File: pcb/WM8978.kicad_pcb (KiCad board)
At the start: 2 copper layers, 1.7 x 7.7 mm, 72 parts, among them CN2 HEADPHONE 3.5mm, J2 JLINK SWD, SW1 RESET, U1 ATSAMD21E18A-A, U15 TLV1117LV33DCYR, U16 WM8978CGEFL/RV, U17 TPS2553DBVR, U18 SN74LVC1G125DBVR, Y1 12MHz / 3.3V / 50ppm

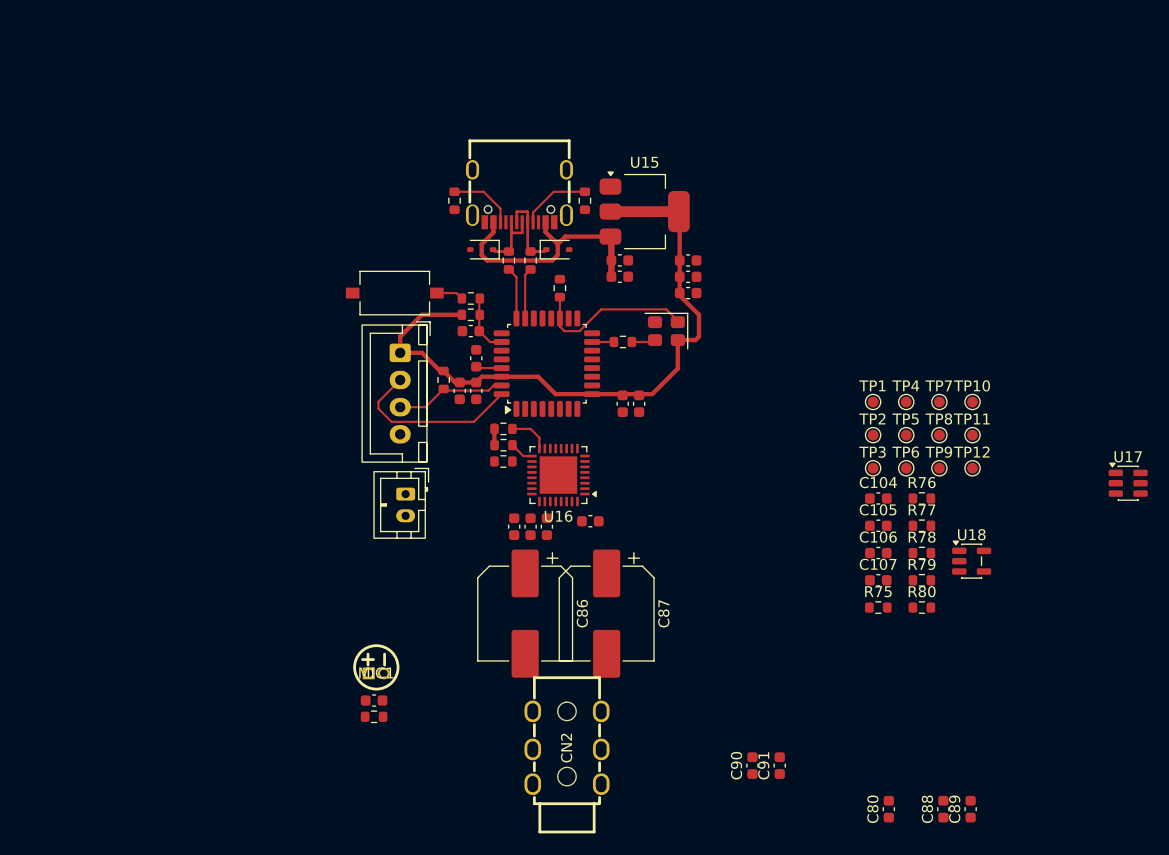
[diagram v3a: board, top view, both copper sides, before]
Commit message: 更新双时钟音频工程并整理中文原理图与检查资料
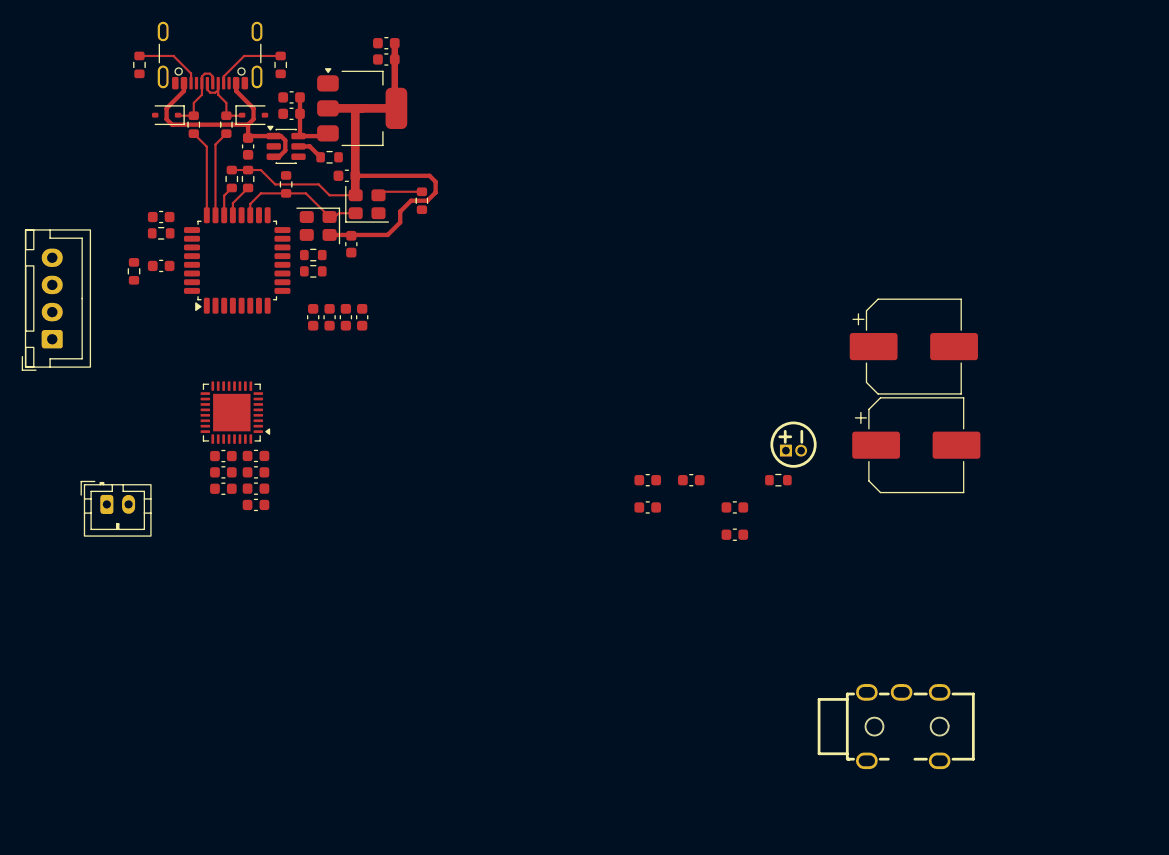
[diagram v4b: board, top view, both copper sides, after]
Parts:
- removed R62: 10k, Resistor_SMD:R_0603_1608Metric
- removed R72: 330R, Resistor_SMD:R_0603_1608Metric
- removed R77: 0R, Resistor_SMD:R_0603_1608Metric
- removed R79, R80: 100k, Resistor_SMD:R_0603_1608Metric
- removed SW1: RESET, Button_Switch_SMD:SW_Tactile_SPST_NO_Straight_CK_PTS636Sx25SMTRLFS
- removed TP1: RESET, TestPoint:TestPoint_Pad_D1.0mm
- removed TP10: SDA, TestPoint:TestPoint_Pad_D1.0mm
- removed TP11: SCL, TestPoint:TestPoint_Pad_D1.0mm
- removed TP12: FAULT, TestPoint:TestPoint_Pad_D1.0mm
- removed TP2: GND, TestPoint:TestPoint_Pad_D1.0mm
- removed TP3: RAW 5V, TestPoint:TestPoint_Pad_D1.0mm
- removed TP4: 5V, TestPoint:TestPoint_Pad_D1.0mm
- removed TP5: 3V3, TestPoint:TestPoint_Pad_D1.0mm
- removed TP6: CORE, TestPoint:TestPoint_Pad_D1.0mm
- removed TP7: MCLK, TestPoint:TestPoint_Pad_D1.0mm
- removed TP8: BCLK, TestPoint:TestPoint_Pad_D1.0mm
- removed TP9: LRCLK, TestPoint:TestPoint_Pad_D1.0mm
- removed U18: SN74LVC1G125DBVR, Package_TO_SOT_SMD:SOT-23-5
- added Y2: 12.288MHz / 3.3V / 50ppm, Oscillator:Oscillator_SMD_Abracon_ASE-4Pin_3.2x2.5mm, F.Cu at (112.0, 46.3)
- USB2: footprint WM8978-import-fps:USB_TYPE-C-16P -> WM8978-import-fps:USB_C_GCT_USB4105_GF_A
- moved U17 83.5 mm to (104.5, 41.0)
- moved C89 71.5 mm to (101.7, 74.0), turned to 0 degrees
- moved C88 69.8 mm to (101.7, 72.5), turned to 0 degrees
- moved C105 67.7 mm to (101.0, 41.0), turned to -90 degrees
- moved R78 65.6 mm to (108.5, 42.0)
- moved R75 60.5 mm to (107.0, 52.5), turned to 180 degrees
- moved R76 60.3 mm to (107.0, 51.0), turned to 180 degrees
- moved C104 57.2 mm to (110.1, 43.7), turned to 180 degrees
- moved C91 55.2 mm to (101.7, 71.0), turned to 0 degrees
- moved C90 53.9 mm to (101.7, 69.5), turned to 0 degrees
- moved MIC1 43.5 mm to (151.2, 69.0)
- moved C86 43.4 mm to (162.3, 59.4), turned to 0 degrees
- moved R68 43.1 mm to (149.8, 71.7), turned to 0 degrees
- moved C80 35.5 mm to (137.8, 74.2), turned to 0 degrees
- moved C77 34.4 mm to (105.0, 36.5), turned to 180 degrees
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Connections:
- C106 pad 1: /AVDD_3V3 -> +3V3
- C107 pad 1: /AVDD_3V3 -> +3V3
- CN2 pad 3: Net-(C87-Pad2) -> Net-(C86-Pad2)
- CN2 pad 4: Net-(C86-Pad2) -> Net-(C87-Pad2)
- R73 pad 1: /MCLK_BUF -> /AUDIO_OSC
- R73 pad 2: /I2S_MCLK -> /AUDIO_MCLK
- U1 pad 15: /I2S_MCLK -> /MCU_12M
- U16 pad 11: /I2S_MCLK -> /AUDIO_MCLK
- U16 pad 18: /MODE -> GND
- U16 pad 31: /AVDD_3V3 -> +3V3
- U17 pad 4: Net-(U17-~{FAULT}) -> unconnected-(U17-~{FAULT}-Pad4)
- Y1 pad 3: /MCLK_XO -> /MCU_12M
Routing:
- net /VBUS_RAW: track 0.00 -> 23.7 mm
- net /VBUS_5V: track 23.6 -> 6.43 mm
- net /SWDIO: track 16.4 -> 0.00 mm
- net /SWCLK: track 10.3 -> 0.00 mm
- net +3V3: track 61.5 -> 53.2 mm
- net /MCU_RESET_N: track 5.50 -> 0.00 mm
- net /AUDIO_OSC: track 0.00 -> 4.13 mm
- net /USB_DP: track 4.80 -> 8.01 mm
- net /USB_DM: track 4.72 -> 7.93 mm
- net /AUDIO_CLK_EN: track 15.1 -> 12.2 mm
- net Net-(R72-Pad2): track 2.51 -> 0.00 mm
- net Net-(U17-ILIM): track 0.00 -> 2.45 mm
- net /VDDCORE: track 2.39 -> 0.00 mm
- net (no net): track 2.20 -> 0.00 mm
- net /I2S_MCLK: track 2.01 -> 0.00 mm
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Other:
- board size 1.7 x 7.7 mm -> 7.7 x 1.7 mm

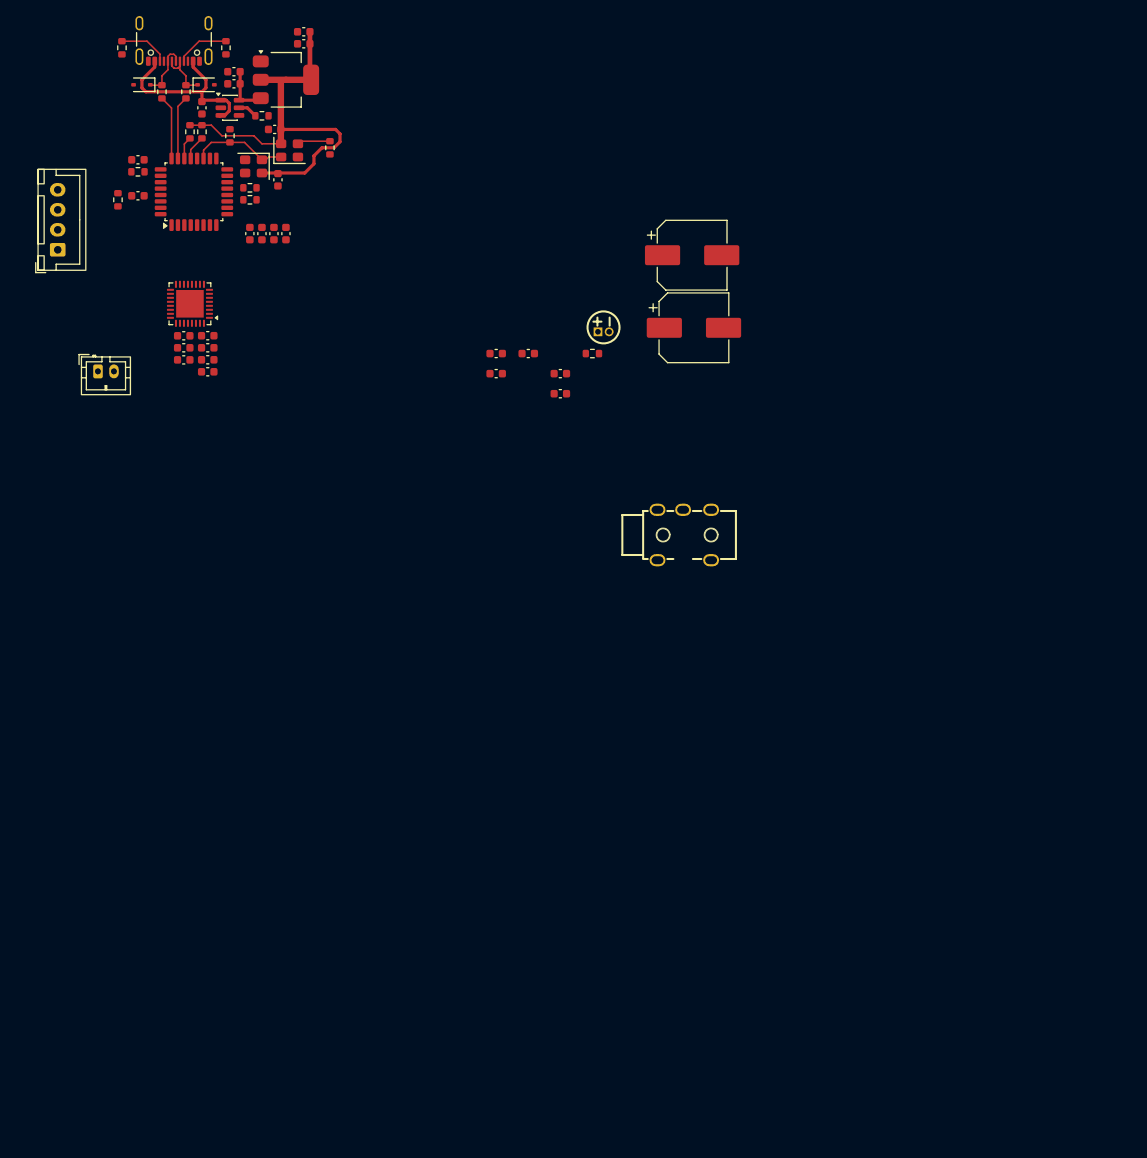
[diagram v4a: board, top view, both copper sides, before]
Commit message: 更新 PCB 布局、走线与铺铜
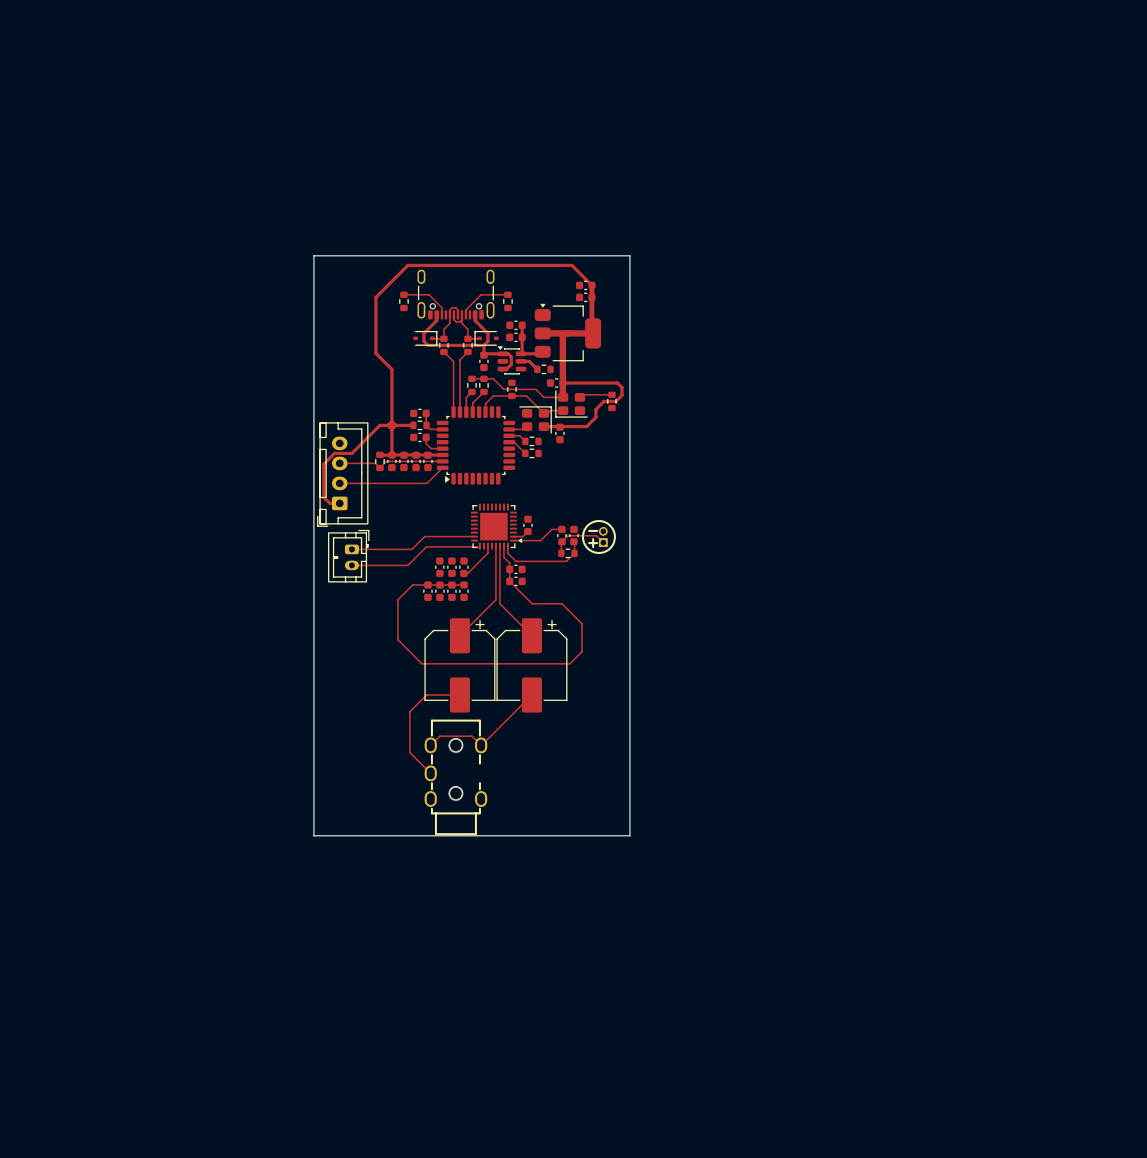
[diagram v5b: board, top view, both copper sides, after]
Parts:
- moved C86 58.9 mm to (133.2, 110.7), turned to -90 degrees
- moved D1 47.4 mm to (128.8, 69.8)
- moved D2 47.4 mm to (136.8, 69.8)
- moved C102 47.4 mm to (128.2, 79.2)
- moved C103 47.4 mm to (145.8, 81.7)
- moved C104 47.4 mm to (145.3, 75.4)
- moved C105 47.4 mm to (136.2, 72.7)
- moved C75 47.4 mm to (140.2, 69.7)
- moved C76 47.4 mm to (149.0, 64.7)
- moved C78 47.4 mm to (149.0, 63.2)
- moved J2 47.4 mm to (118.2, 90.5)
- moved R53 47.4 mm to (131.2, 70.7)
- moved R54 47.4 mm to (134.2, 70.7)
- moved R63 47.4 mm to (136.2, 75.7)
- moved R64 47.4 mm to (134.8, 75.7)
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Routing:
- net +3V3: track 53.2 -> 192.1 mm
- net Net-(U16-LOUT2): track 0.00 -> 16.8 mm
- net Net-(C87-Pad2): track 0.00 -> 16.2 mm
- net Net-(U16-ROUT2): track 0.00 -> 16.0 mm
- net Net-(C86-Pad2): track 0.00 -> 15.9 mm
- net /SWDIO: track 0.00 -> 13.7 mm
- net /SWCLK: track 0.00 -> 13.4 mm
- net Net-(U16-ROUT1): track 0.00 -> 13.1 mm
- net Net-(U16-LOUT1): track 0.00 -> 12.9 mm
- net /MICBIAS: track 0.00 -> 11.5 mm
- net Net-(C79-Pad2): track 0.00 -> 7.32 mm
- net /MIC_LIP: track 0.00 -> 6.64 mm
- net Net-(U16-VMID): track 0.00 -> 4.93 mm
- net /MCU_RESET_N: track 0.00 -> 3.74 mm
- net /VDDCORE: track 0.00 -> 3.10 mm
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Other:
- board size 7.7 x 1.7 mm -> 39.5 x 72.5 mm

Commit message: 9.23
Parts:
- moved C89 13.2 mm to (137.0, 90.7), turned to 90 degrees
- moved C88 11.7 mm to (135.5, 90.7), turned to 90 degrees
- moved C91 10.9 mm to (134.0, 90.7), turned to 90 degrees
- moved C90 10.8 mm to (132.5, 90.7), turned to 90 degrees
- moved C103 4.87 mm to (150.2, 79.7), turned to 90 degrees
- moved C106 3.00 mm to (140.2, 101.7)
- moved C107 3.00 mm to (140.2, 103.2)
- moved C79 3.00 mm to (146.0, 97.5)
- moved C80 3.00 mm to (141.8, 96.2)
- moved C83 3.00 mm to (133.8, 101.4)
- moved C86 3.00 mm to (133.2, 113.7)
- moved C87 3.00 mm to (142.2, 113.7)
- moved C92 3.00 mm to (132.2, 101.4)
- moved C93 3.00 mm to (130.7, 101.4)
- moved C96 3.00 mm to (147.5, 97.5)
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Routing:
- net +3V3: track 192.1 -> 246.1 mm
- net /VBUS_5V: track 6.43 -> 56.5 mm, vias 0 -> 2
- net /AUDIO_MCLK: track 0.00 -> 25.6 mm, vias 0 -> 2
- net /CODEC_SDA: track 3.09 -> 21.3 mm, vias 0 -> 2
- net /CODEC_SCL: track 2.80 -> 18.8 mm, vias 0 -> 2
- net /CODEC_LRCLK: track 0.00 -> 15.8 mm
- net /CODEC_BCLK: track 0.00 -> 11.7 mm
- net /I2S_ADCDAT: track 0.00 -> 11.4 mm
- net /I2S_DACDAT: track 0.00 -> 6.84 mm
- net GND: track 0.00 -> 4.19 mm, vias 0 -> 247
- net Net-(U16-LOUT2): track 16.8 -> 16.2 mm
- net Net-(C86-Pad2): track 15.9 -> 16.5 mm
- added copper zone on B.Cu, net GND
- added copper zone on F.Cu, net GND
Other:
- board size 39.5 x 72.5 mm -> 39.5 x 74.8 mm

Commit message: 更新 PCB 布局并同步复核资料
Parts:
- moved C99 16.4 mm to (141.0, 87.5), turned to 0 degrees
- moved R76 12.8 mm to (142.2, 95.5), turned to 0 degrees
- moved C100 12.3 mm to (141.0, 89.0), turned to 0 degrees
- moved R75 9.80 mm to (142.2, 94.0), turned to 0 degrees
- moved C80 1.92 mm to (141.5, 98.1), turned to -90 degrees
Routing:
- net /I2S_LRCLK: track 2.30 -> 18.8 mm
- net /CODEC_LRCLK: track 15.8 -> 1.65 mm
- net /I2S_BCLK: track 2.59 -> 14.0 mm
- net /CODEC_BCLK: track 11.7 -> 1.74 mm
- net +3V3: track 246.1 -> 249.3 mm
- net GND: vias 247 -> 277

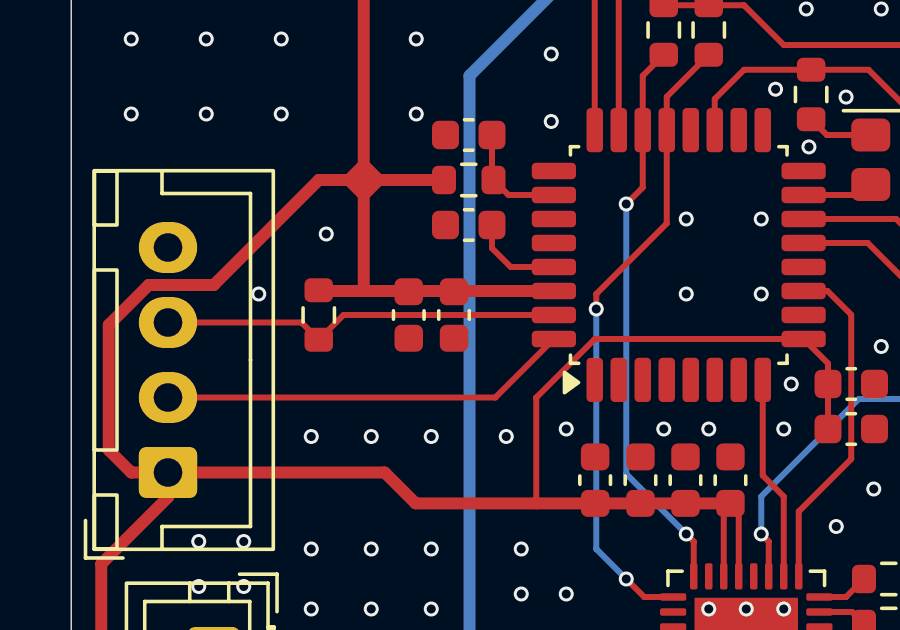
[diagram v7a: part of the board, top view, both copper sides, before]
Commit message: 补齐封装关联并绑定原始 3D 模型
补齐 C97～C100 的符号关联，Y1/Y2 使用 Abracon 原厂 STEP，MIC1 使用立创原库 STEP。
CN2 保留现有五脚封装，仅去除原库 CAD 多余的板下插脚，并保存未经修改的六脚原文件。
保留最新存档中的 C97/C98 位置与铺铜调整，记录 54 个器件的关联、模型及原生 STEP 验证结果。
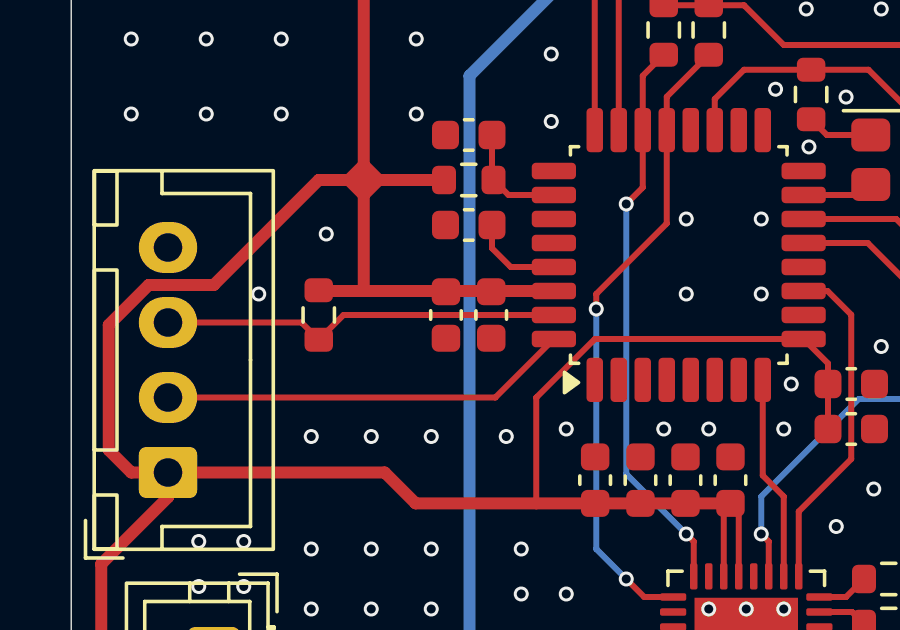
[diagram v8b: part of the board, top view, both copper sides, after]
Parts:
- Y1, Y2: footprint Oscillator:Oscillator_SMD_Abracon_ASE-4Pin_3.2x2.5mm -> WM8978-import-fps:Oscillator_SMD_Abracon_ASE-4Pin_3.2x2.5mm
- moved C97 1.24 mm to (129.0, 85.2)
- moved C98 1.24 mm to (127.5, 85.2)
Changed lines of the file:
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@@
 		)
 	)
-	(footprint "Oscillator:Oscillator_SMD_Abracon_ASE-4Pin_3.2x2.5mm"
+	(footprint "WM8978-import-fps:Oscillator_SMD_Abracon_ASE-4Pin_3.2x2.5mm"
 		(layer "F.Cu")
 		(at 147.2 78.025)
@@
 		)
 		(embedded_fonts no)
-		(model "${KICAD10_3DMODEL_DIR}/Oscillator.3dshapes/Oscillator_SMD_Abracon_ASE-4Pin_3.2x2.5mm.step"
+		(model "${KIPRJMOD}/WM8978.3dshapes/ASE.step"
 			(offset
-				(xyz 0 0 0)
+				(xyz 0 0 0.5501)
 			)
 			(scale
@@
 		)
 		(embedded_fonts no)
-		(model "${KIPRJMOD}/EASYEDA_MODELS/MIC-TH_BD4.0-P1.40-D0.4-L-FD.step"
+		(model "${KIPRJMOD}/WM8978.3dshapes/MIC-TH_BD4.0-P1.40-D0.4-L-FD.step"
 			(offset
-				(xyz 0 0.553 -3)
+				(xyz 0 0.55 0)
 			)
 			(scale
@@
 			)
 			(rotate
-				(xyz -0 -0 -0)
+				(xyz 0 0 0)
 			)
 		)
@@
 		)
 		(embedded_fonts no)
-		(model "${KIPRJMOD}/EASYEDA_MODELS/AUDIO-TH_PJ-3136-B.step"
+		(model "${KIPRJMOD}/WM8978.3dshapes/AUDIO-TH_PJ-3136-B_5pin.step"
 			(offset
-				(xyz -0.65 0 -3)
+				(xyz -0.65 0 0)
 			)
 			(scale
@@
 			)
 			(rotate
-				(xyz -0 -0 -0)
+				(xyz 0 0 0)
 			)
 		)
@@
 	(footprint "Capacitor_SMD:C_0603_1608Metric"
 		(layer "F.Cu")
-		(at 126.25 85.2 -90)
+		(at 127.49 85.2 -90)
 		(descr "Capacitor SMD 0603 (1608 Metric), square (rectangular) end terminal, IPC-7351 nominal, (Body size source: IPC-SM-782 page 76, https://www.pcb-3d.com/wordpress/wp-content/uploads/ipc-sm-782a_amendment_1_and_2.pdf)")
 		(tags "capacitor")
@@
 	(footprint "Capacitor_SMD:C_0603_1608Metric"
 		(layer "F.Cu")
-		(at 127.76 85.2 -90)
+		(at 129 85.2 -90)
 		(descr "Capacitor SMD 0603 (1608 Metric), square (rectangular) end terminal, IPC-7351 nominal, (Body size source: IPC-SM-782 page 76, https://www.pcb-3d.com/wordpress/wp-content/uploads/ipc-sm-782a_amendment_1_and_2.pdf)")
 		(tags "capacitor")
@@
 		)
 	)
-	(footprint "Oscillator:Oscillator_SMD_Abracon_ASE-4Pin_3.2x2.5mm"
+	(footprint "WM8978-import-fps:Oscillator_SMD_Abracon_ASE-4Pin_3.2x2.5mm"
 		(layer "F.Cu")
 		(at 142.7 80.025 180)
@@
 		)
 		(embedded_fonts no)
-		(model "${KICAD10_3DMODEL_DIR}/Oscillator.3dshapes/Oscillator_SMD_Abracon_ASE-4Pin_3.2x2.5mm.step"
+		(model "${KIPRJMOD}/WM8978.3dshapes/ASE.step"
 			(offset
-				(xyz 0 0 0)
+				(xyz 0 0 0.5501)
 			)
 			(scale
